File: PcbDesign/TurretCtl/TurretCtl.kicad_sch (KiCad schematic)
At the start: 7 parts, among them J1 PWR, J2 St1, J3 St2, J4 Sv1, J5 Sense, J6 Sv2

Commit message: TurretCtl revision
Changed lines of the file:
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@@
     (effects (font (size 1.27 1.27)) (justify left bottom))
   )
-  (label "Step1" (at 102.87 85.09 0) (fields_autoplaced)
+  (label "Step2" (at 102.87 85.09 0) (fields_autoplaced)
     (effects (font (size 1.27 1.27)) (justify left bottom))
   )
@@
     (effects (font (size 1.27 1.27)) (justify left bottom))
   )
-  (label "Dir1" (at 102.87 82.55 0) (fields_autoplaced)
+  (label "Dir2" (at 102.87 82.55 0) (fields_autoplaced)
     (effects (font (size 1.27 1.27)) (justify left bottom))
   )

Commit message: TurretCtl V2
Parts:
- removed J1: PWR, TerminalBlock_Phoenix:TerminalBlock_Phoenix_PTSM-0,5-4-2.5-H-THR_1x04_P2.50mm_Horizontal, symbol Connector_Generic:Conn_01x04
- removed J2: St1, TerminalBlock_Phoenix:TerminalBlock_Phoenix_PTSM-0,5-4-2.5-H-THR_1x04_P2.50mm_Horizontal, symbol Connector_Generic:Conn_01x04
- removed J3: St2, TerminalBlock_Phoenix:TerminalBlock_Phoenix_PTSM-0,5-4-2.5-H-THR_1x04_P2.50mm_Horizontal, symbol Connector_Generic:Conn_01x04
- removed J4: Sv1, TerminalBlock_Phoenix:TerminalBlock_Phoenix_PTSM-0,5-4-2.5-H-THR_1x04_P2.50mm_Horizontal, symbol Connector_Generic:Conn_01x04
- removed J5: Sense, TerminalBlock_Phoenix:TerminalBlock_Phoenix_PTSM-0,5-4-2.5-H-THR_1x04_P2.50mm_Horizontal, symbol Connector_Generic:Conn_01x04
- removed J6: Sv2, TerminalBlock_Phoenix:TerminalBlock_Phoenix_PTSM-0,5-4-2.5-H-THR_1x04_P2.50mm_Horizontal, symbol Connector_Generic:Conn_01x04
- added C15: 680uF, symbol Device:C_Small
- added J1: Conn_01x06, symbol Connector_Generic:Conn_01x06
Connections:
- net GND: now also C15.2, J1.6 (Pin_6); no longer A1.29 (GND), A1.6 (GND), A1.7 (GND)
- net SDA: now reaches A1.31 (SDA/A4)
- net SDA: now also J1.5 (Pin_5)
- net SCL: now reaches A1.32 (SCL/A5)
- net SCL: now also J1.4 (Pin_4)
- net Dir1: no longer names the net of A1.17 (D2)
- net Dir2: no longer names the net of A1.19 (D4)
- net Sig1: no longer names the net of A1.24 (D9)
- net Sig2: no longer names the net of A1.23 (D8)
- net Step1: no longer names the net of A1.18 (D3)
- net Step2: no longer names the net of A1.20 (D5)
- net Sw-I: no longer names the net of A1.22 (D7)
- net Sw-O: no longer names the net of A1.5 (+5V)
- net VM: no longer names the net of A1.8 (VIN)
- new net +5V: C15.1, J1.1 (Pin_1)
- no-connect marks 0 -> 2
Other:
- sheet Stepper1: file DRV8886.kicad_sch -> StepperCtl.kicad_sch
- sheet Stepper1 ports: added none; removed GND, VM
- sheet Stepper2: file DRV8886.kicad_sch -> StepperCtl.kicad_sch
- sheet Stepper2 ports: added none; removed GND, VM

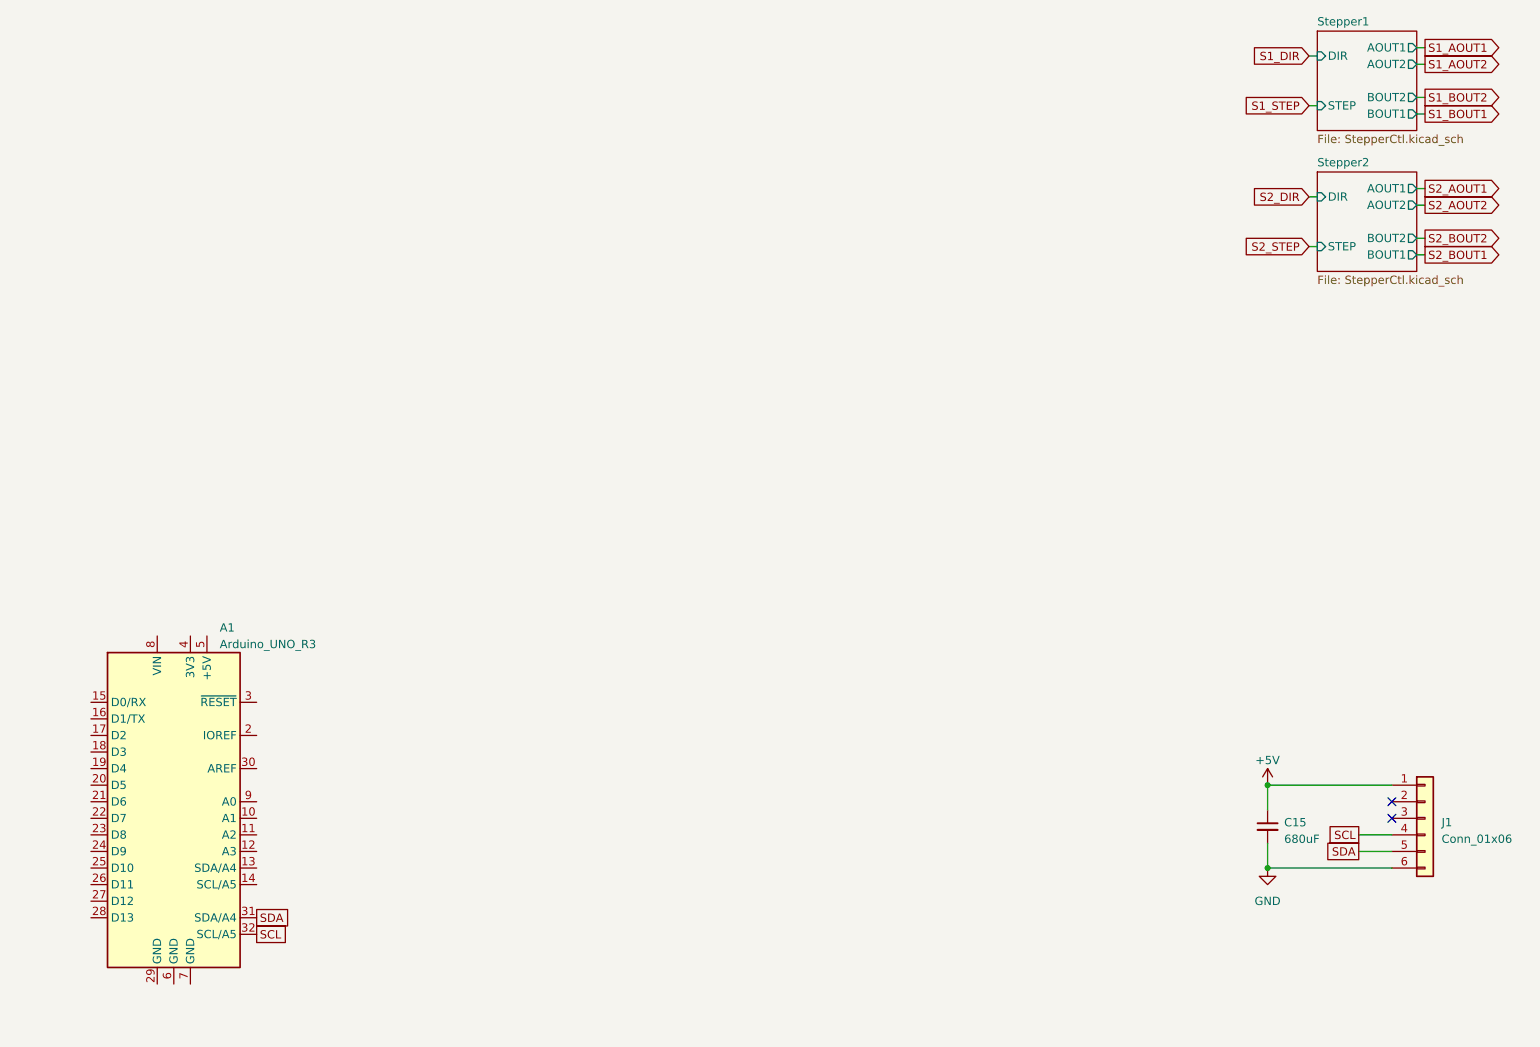
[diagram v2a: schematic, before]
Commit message: Foot print selection
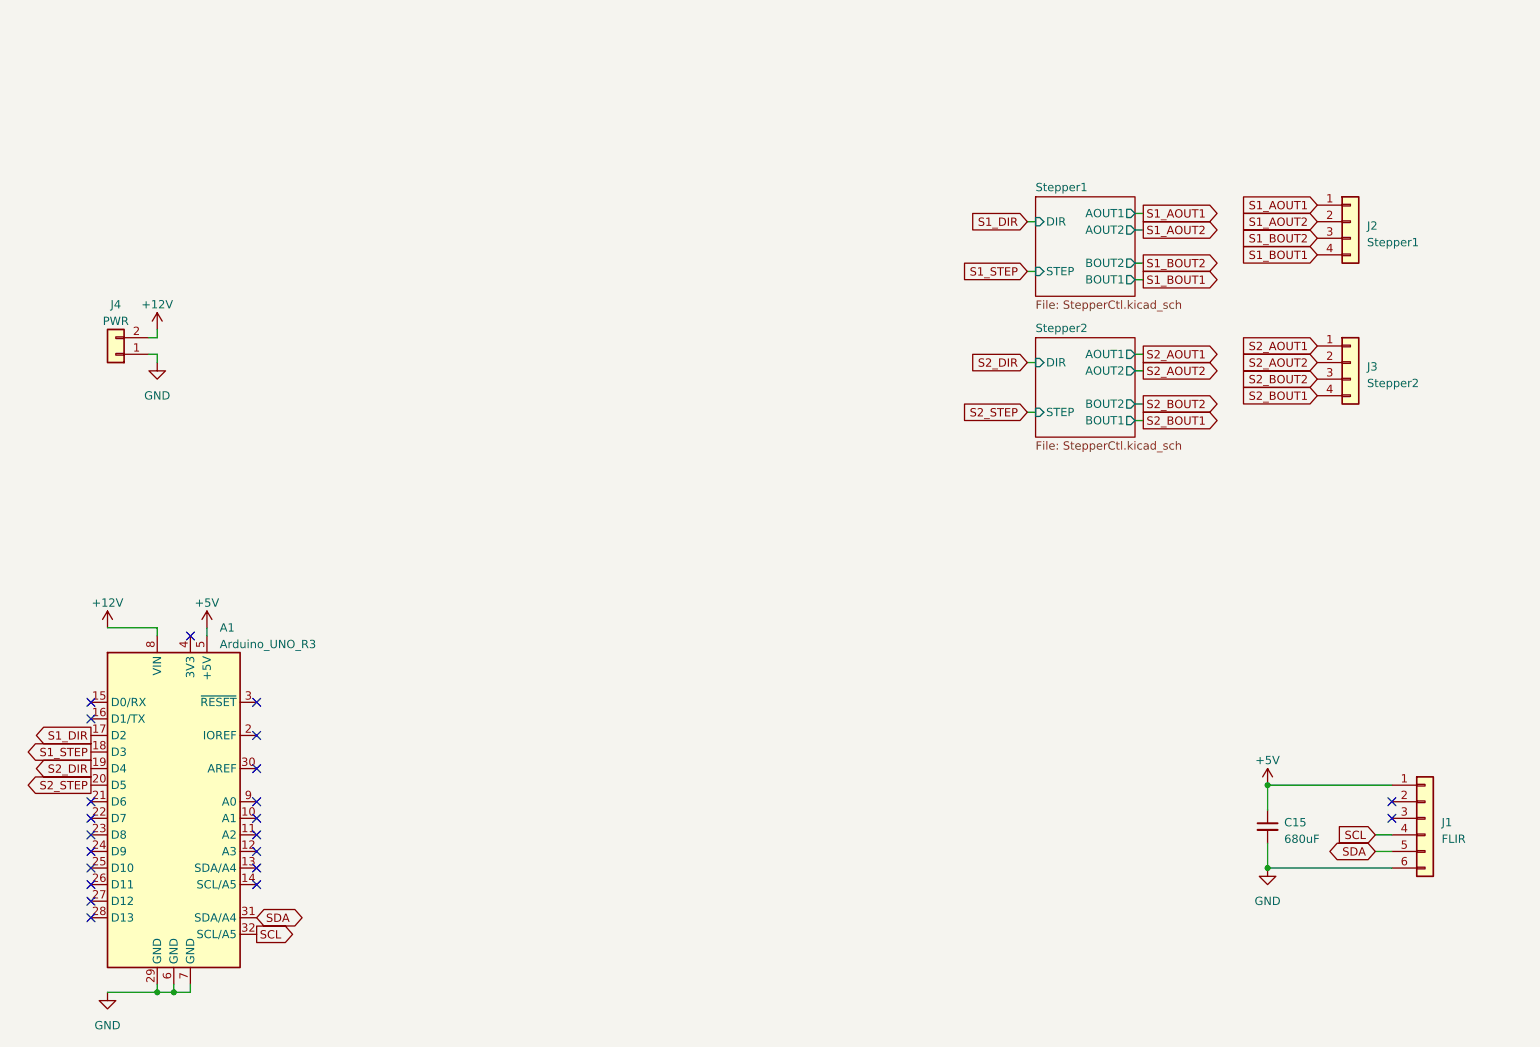
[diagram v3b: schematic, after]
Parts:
- added J2: Stepper1, symbol Connector_Generic:Conn_01x04
- added J3: Stepper2, symbol Connector_Generic:Conn_01x04
- added J4: PWR, symbol Connector_Generic:Conn_01x02
- C15: footprint (none) -> Capacitor_THT:C_Radial_D10.0mm_H16.0mm_P5.00mm
- J1: value Conn_01x06 -> FLIR
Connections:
- net +5V: now also A1.5 (+5V)
- net GND: now also A1.29 (GND), A1.6 (GND), A1.7 (GND), J4.1 (Pin_1)
- net S1_AOUT1: now also J2.1 (Pin_1)
- net S1_AOUT2: now also J2.2 (Pin_2)
- net S1_BOUT1: now also J2.4 (Pin_4)
- net S1_BOUT2: now also J2.3 (Pin_3)
- net S1_DIR: now also A1.17 (D2)
- net S1_STEP: now also A1.18 (D3)
- net S2_AOUT1: now also J3.1 (Pin_1)
- net S2_AOUT2: now also J3.2 (Pin_2)
- net S2_BOUT1: now also J3.4 (Pin_4)
- net S2_BOUT2: now also J3.3 (Pin_3)
- net S2_DIR: now also A1.19 (D4)
- net S2_STEP: now also A1.20 (D5)
- net +12V: now reaches A1.8 (VIN)
- net +12V: now also J4.2 (Pin_2)
- no-connect marks 2 -> 22

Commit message: Reader for JLCPCB run
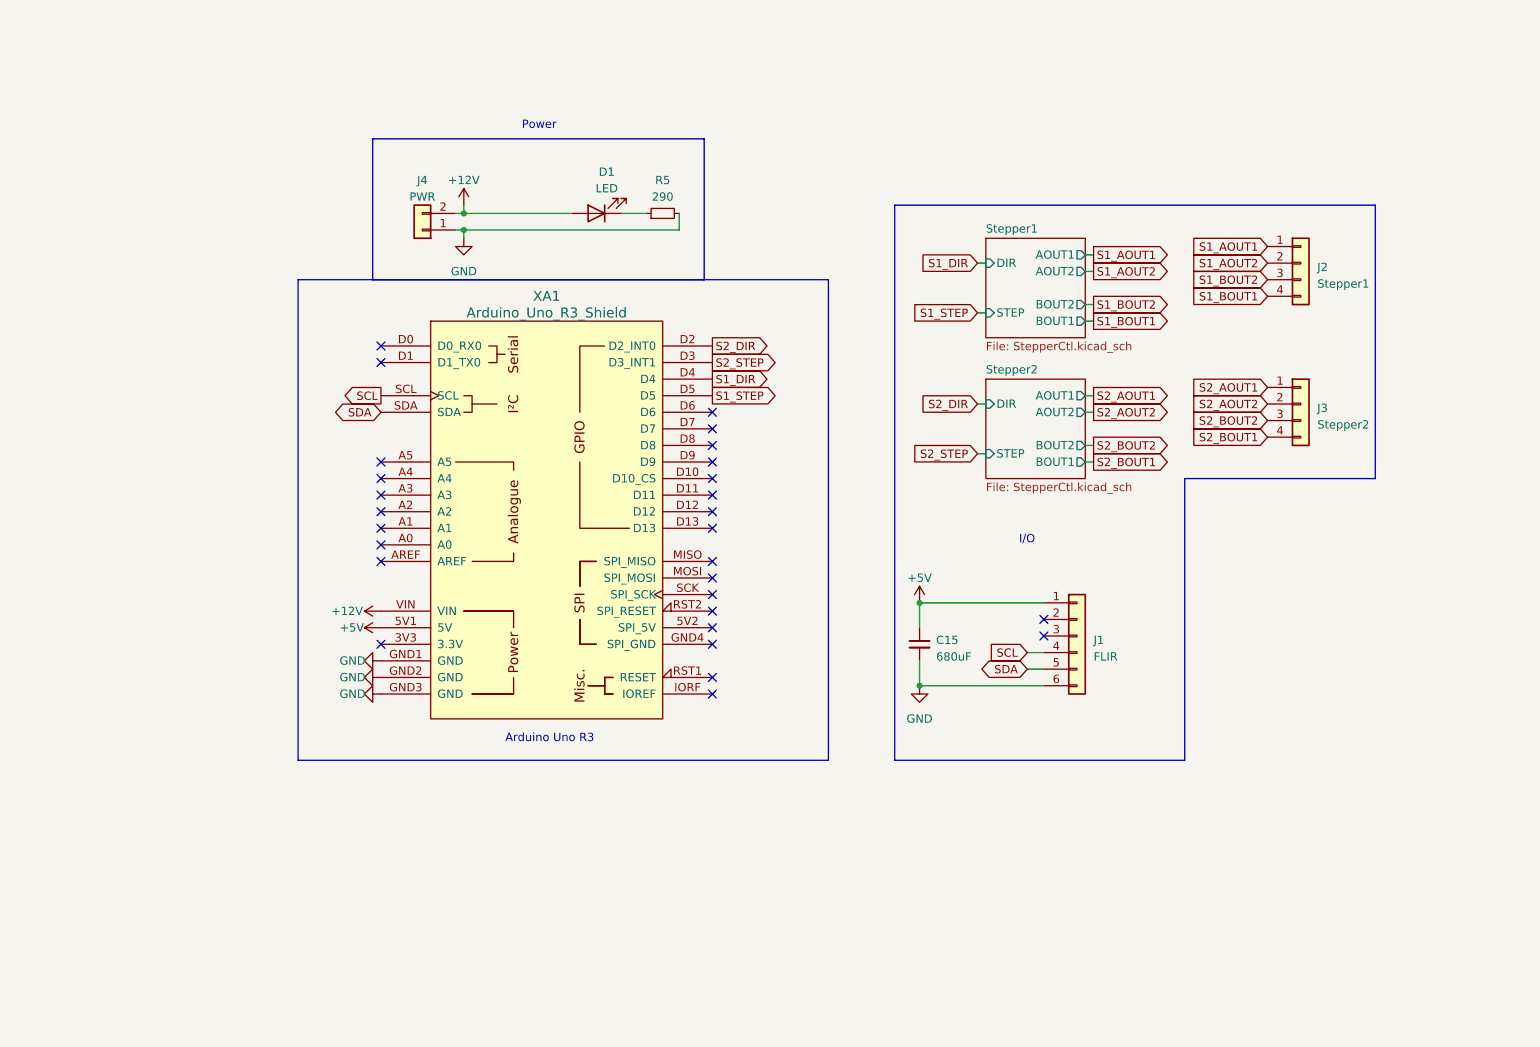
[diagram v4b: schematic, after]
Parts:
- removed A1: Arduino_UNO_R3, Module:Arduino_UNO_R3, symbol MCU_Module:Arduino_UNO_R3
- added D1: LED, LED_SMD:LED_0603_1608Metric, symbol Device:LED
- added R5: 290, Resistor_SMD:R_0402_1005Metric, symbol Device:R_Small
- added XA1: Arduino_Uno_R3_Shield, arduino-library:Arduino_Uno_R3_Shield, symbol arduino-library:Arduino_Uno_R3_Shield
- C15: footprint Capacitor_THT:C_Radial_D10.0mm_H16.0mm_P5.00mm -> Capacitor_THT:C_Radial_D8.0mm_H11.5mm_P3.50mm; LCSC Part (none) -> C88760; LCSC Part # (none) -> C88760
- J1: footprint (none) -> Connector_JST:JST_GH_SM06B-GHS-TB_1x06-1MP_P1.25mm_Horizontal; LCSC Part (none) -> C133065; LCSC Part # (none) -> C133065
- J2, J3: footprint (none) -> Connector_Phoenix_MC:PhoenixContact_MCV_1,5_4-G-3.5_1x04_P3.50mm_Vertical
- J4: footprint (none) -> Connector_Phoenix_MC:PhoenixContact_MC_1,5_2-G-3.5_1x02_P3.50mm_Horizontal
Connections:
- net +12V: now also D1.2 (A), XA1.VIN
- net +5V: now also XA1.5V1 (5V)
- net GND: now also R5.2, XA1.GND1 (GND), XA1.GND2 (GND), XA1.GND3 (GND)
- net S1_DIR: now also XA1.D4
- net S1_STEP: now also XA1.D5
- net S2_DIR: now also XA1.D2 (D2_INT0)
- net S2_STEP: now also XA1.D3 (D3_INT1)
- net SCL: now also XA1.SCL
- net SDA: now also XA1.SDA
- new net: D1.1 (K), R5.1
- no-connect marks 22 -> 28
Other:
- note added: "Arduino Uno R3"
- note added: "I/O"
- note added: "Power"
- moved on the sheet: C15, J1, J2, J3, J4

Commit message: Stepper Control Board V2
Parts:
- added D14, D15, D18, D19: LED, LED_SMD:LED_0603_1608Metric, symbol Device:LED
- added J5: Sensors, Connector_JST:JST_GH_SM06B-GHS-TB_1x06-1MP_P1.25mm_Horizontal, symbol Connector_Generic:Conn_01x06
- added R18, R19, R22, R23: 330, Resistor_SMD:R_0402_1005Metric, symbol Device:R_Small
- R5: value 290 -> 330
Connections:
- net +5V: now also D14.2 (A), J5.1 (Pin_1), J5.3 (Pin_3), J5.5 (Pin_5)
- net GND: now also R18.2, R19.2, R22.2, R23.2
- net D6: now reaches XA1.D6
- net D6: now also D15.2 (A), J5.6 (Pin_6)
- net D7: now reaches XA1.D7
- net D7: now also D18.2 (A), J5.4 (Pin_4)
- net D8: now reaches XA1.D8
- net D8: now also D19.2 (A), J5.2 (Pin_2)
- new net: D15.1 (K), R19.1
- new net: D18.1 (K), R22.1
- new net: D14.1 (K), R18.1
- new net: D19.1 (K), R23.1
- no-connect marks 28 -> 25
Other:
- moved on the sheet: C15, D1, J1, J4, R5

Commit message: New connectors
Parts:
- added D10, D11, D20: LED, LED_SMD:LED_0603_1608Metric, symbol Device:LED
- added R14, R15, R24: 330, Resistor_SMD:R_0402_1005Metric, symbol Device:R_Small
- J1, J5: footprint Connector_JST:JST_GH_SM06B-GHS-TB_1x06-1MP_P1.25mm_Horizontal -> Connector_Phoenix_MC:PhoenixContact_MCV_1,5_6-G-3.5_1x06_P3.50mm_Vertical
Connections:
- net GND: now also D10.2 (A), R14.2, R15.2, R24.2
- net SCL: now also D20.2 (A)
- net SDA: now also D11.2 (A)
- new net: D11.1 (K), R15.1
- new net: D20.1 (K), R24.1
- new net: D10.1 (K), R14.1
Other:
- moved on the sheet: C15, J1

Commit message: Control board v3
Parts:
- added D21, D22: LED, LED_SMD:LED_0603_1608Metric, symbol Device:LED
- added R25, R26: 330, Resistor_SMD:R_0402_1005Metric, symbol Device:R_Small
- J1, J5: LCSC Part C133065 -> (none); LCSC Part # C133065 -> (none)
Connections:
- net GND: now also R25.2, R26.2; no longer D10.2 (A)
- net S1_DIR: now also D22.2 (A)
- net S1_STEP: now also D21.2 (A)
- net S2_DIR: now also D20.2 (A)
- net S2_STEP: now also D11.2 (A)
- net SCL: no longer D20.2 (A)
- net SDA: no longer D11.2 (A)
- net at XA1.D9: now also D10.2 (A)
- new net: D22.1 (K), R26.1
- new net: D21.1 (K), R25.1
- no-connect marks 25 -> 24
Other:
- moved on the sheet: D10, J2, J3, R14
